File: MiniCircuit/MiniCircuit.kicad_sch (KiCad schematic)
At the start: 32 parts, among them IC1 MAX4737EUD+, IC2 MAX4737EUD+, IC3 MAX4737EUD+, IC4 MAX4737EUD+, J1 Conn_02x16_Odd_Even, J2 Conn_01x08, SW1 SW_DIP_x08, U1 LM6172, U2 OPA2277, U3 MCP3008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

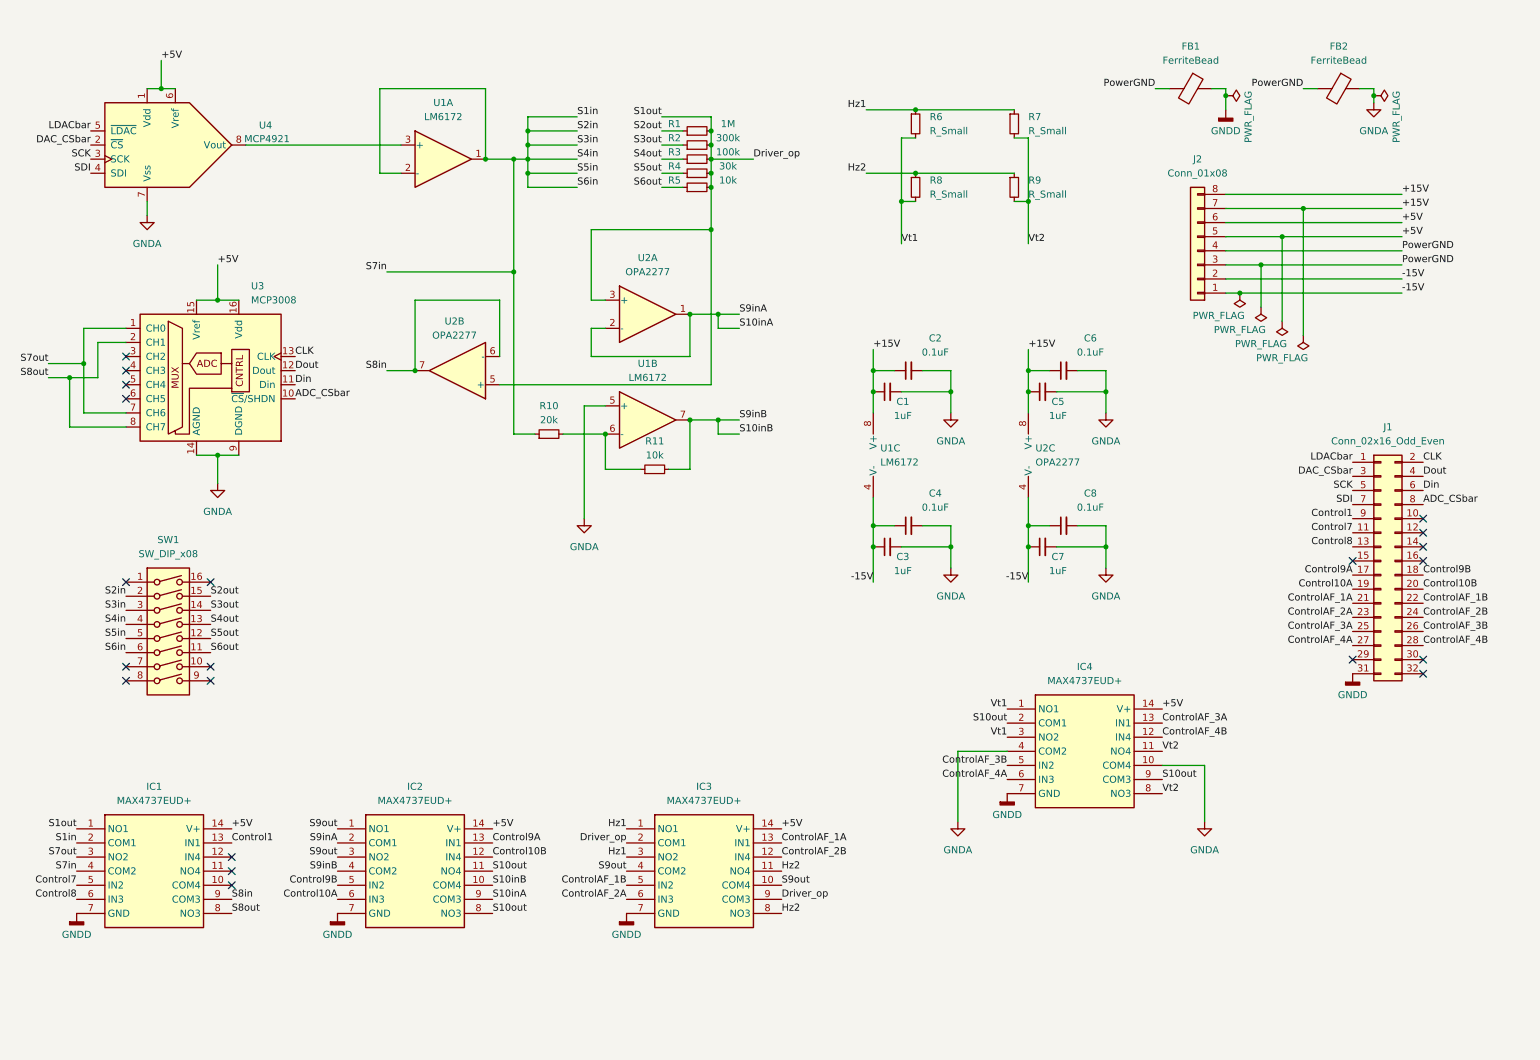
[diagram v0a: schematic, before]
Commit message: Everything done except routing of digital signals and adding Vias
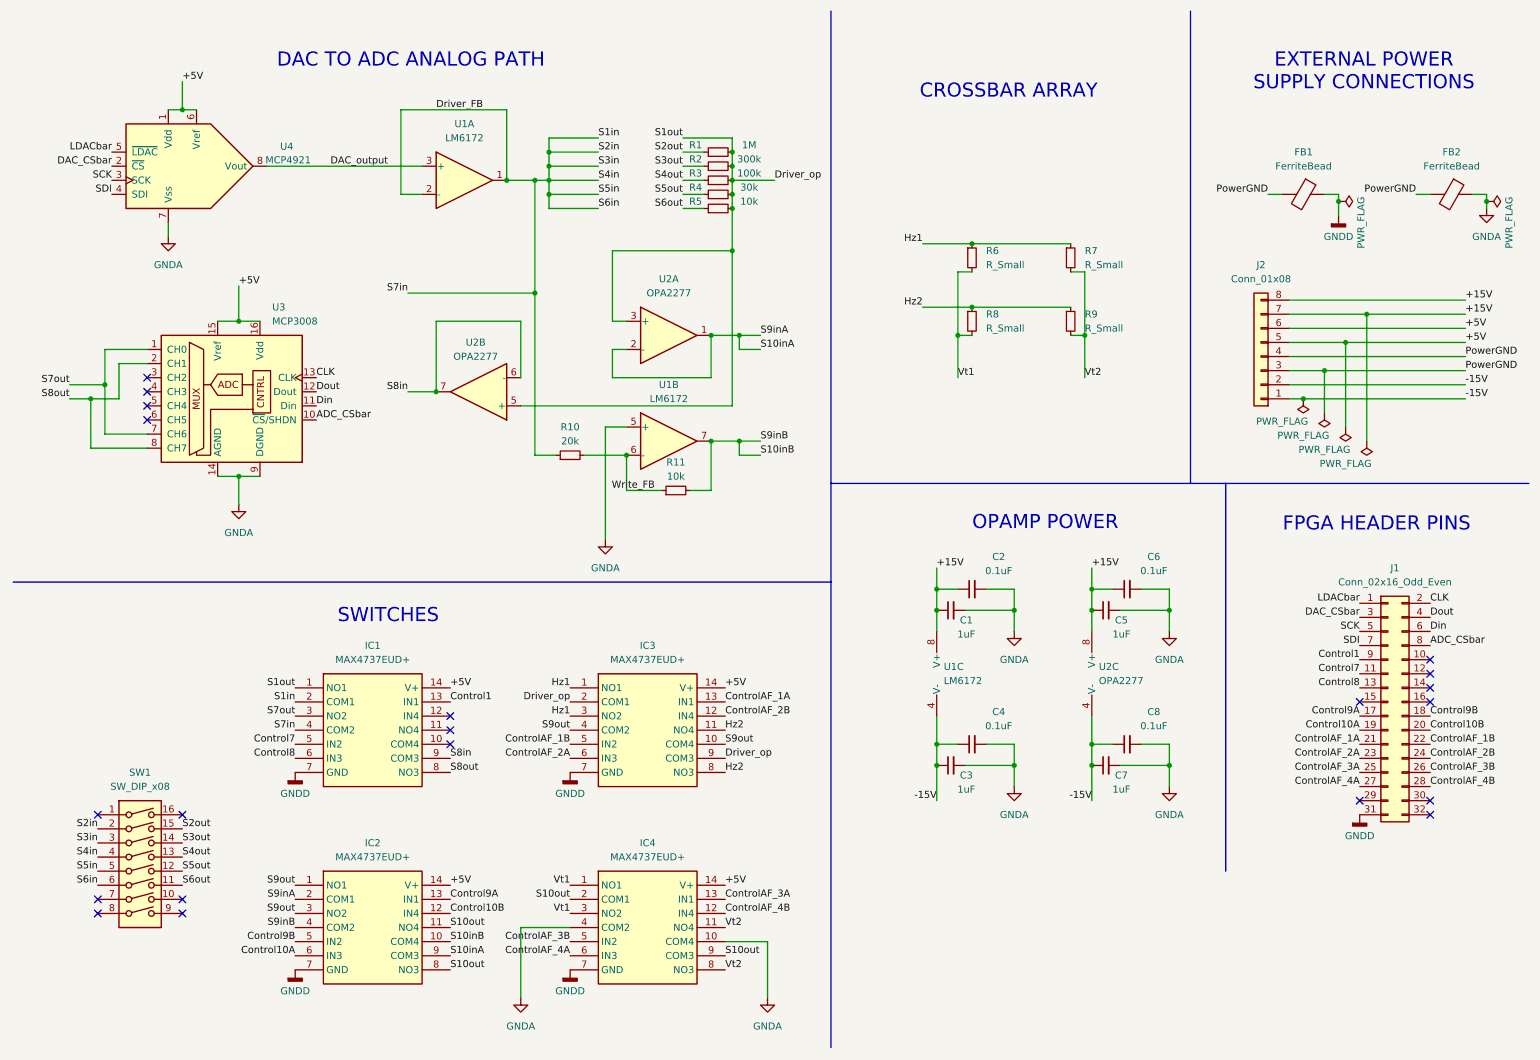
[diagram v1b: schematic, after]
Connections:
- net DAC_output: now reaches U1.3 (+), U4.8 (Vout)
- net Write_FB: now reaches R10.2, R11.1, U1.6 (-)
- net S1in renamed Driver_FB
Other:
- note added: "CROSSBAR ARRAY"
- note added: "DAC TO ADC ANALOG PATH"
- note added: "EXTERNAL POWER SUPPLY CONNECTIONS"
- note added: "FPGA HEADER PINS"
- note added: "OPAMP POWER"
- note added: "SWITCHES"
- moved on the sheet: C1, C2, C3, C4, C5, C6, C7, C8, FB1, FB2, IC1, IC2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

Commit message: Changed Schematic to include CD4066 instead of MAX4737. Design Constraints, Routing and Layout remaining
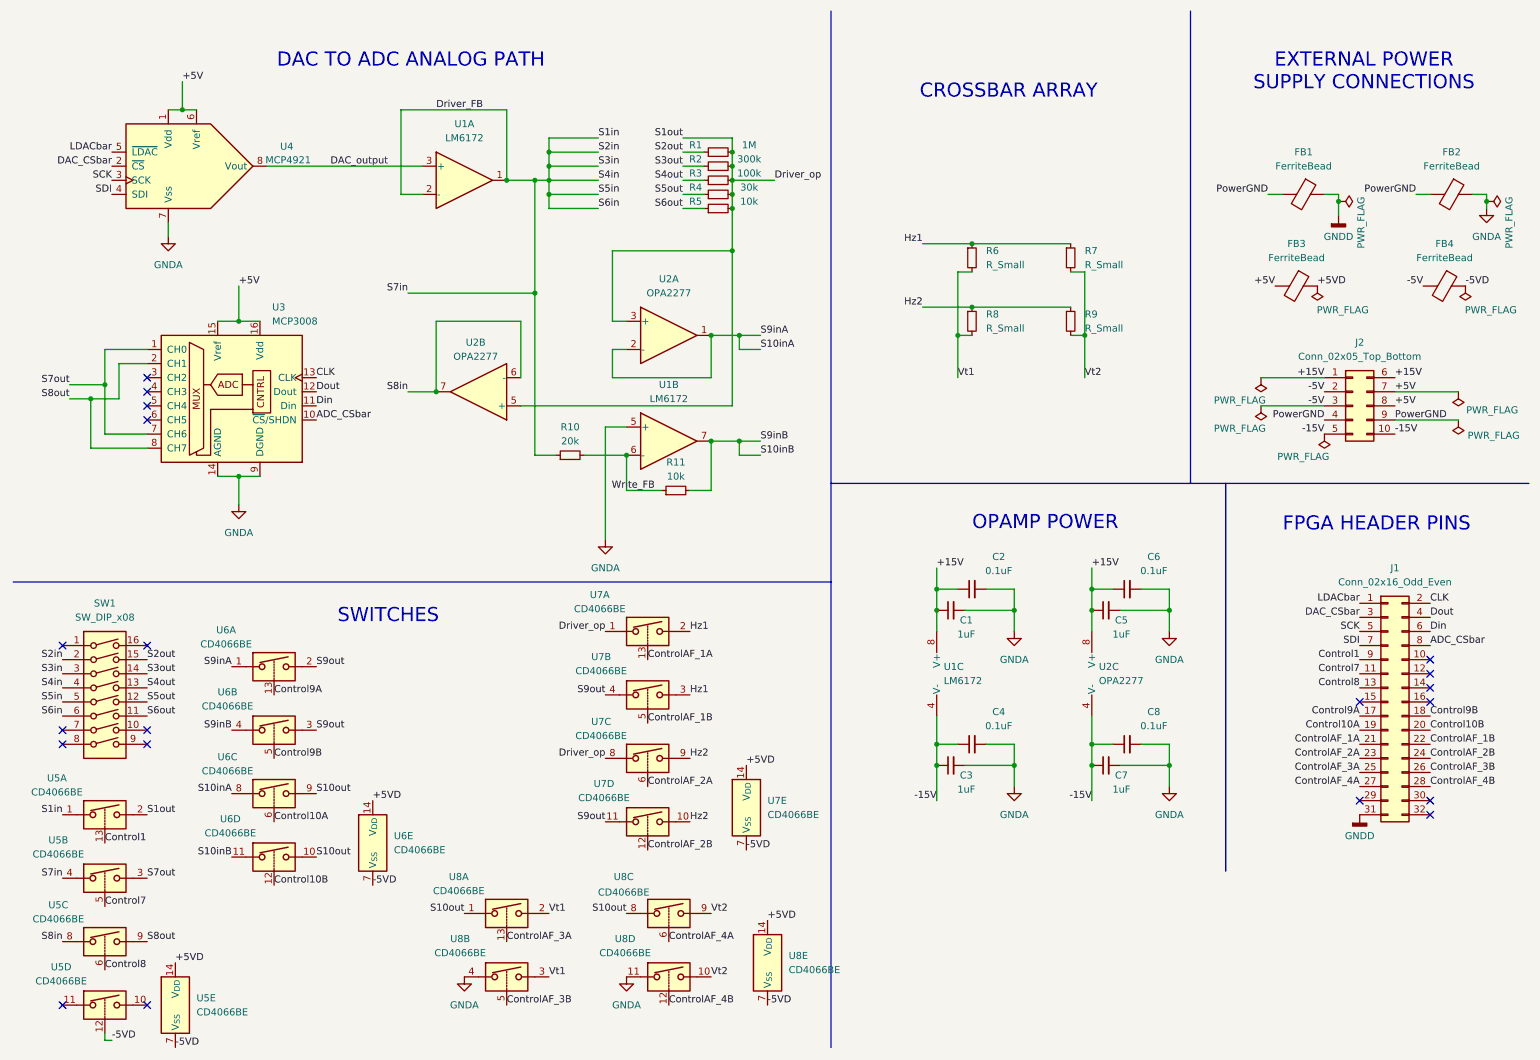
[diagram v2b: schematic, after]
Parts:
- removed IC1, IC2, IC3, IC4: MAX4737EUD+, MAX4737:SOP65P640X110-14N, symbol MAX4737:MAX4737EUD+
- removed J2: Conn_01x08, Connector_PinHeader_2.54mm:PinHeader_1x08_P2.54mm_Vertical, symbol Connector_Generic:Conn_01x08
- added FB3, FB4: FerriteBead, Inductor_SMD:L_1206_3216Metric_Pad1.22x1.90mm_HandSolder, symbol Device:FerriteBead
- added J2: Conn_02x05_Top_Bottom, Connector_PinHeader_2.54mm:PinHeader_2x05_P2.54mm_Vertical, symbol Connector_Generic:Conn_02x05_Top_Bottom
- added U5, U6, U7, U8: CD4066BE, Package_DIP:DIP-14_W7.62mm_Socket, symbol Analog_Switch:CD4066BE
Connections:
- net +15V: now also J2.1 (Pin_1), J2.6 (Pin_6)
- net +5V: now also FB3.2, J2.7 (Pin_7), J2.8 (Pin_8)
- net -15V: now also J2.10 (Pin_10), J2.5 (Pin_5)
- net Control1: now also U5.13
- net Control10A: now also U6.6
- net Control10B: now also U6.12
- net Control7: now also U5.5
- net Control8: now also U5.6
- net Control9A: now also U6.13
- net Control9B: now also U6.5
- net ControlAF_1A: now also U7.13
- net ControlAF_1B: now also U7.5
- net ControlAF_2A: now also U7.6
- net ControlAF_2B: now also U7.12
- net ControlAF_3A: now also U8.13
- net ControlAF_3B: now also U8.5
- net ControlAF_4A: now also U8.6
- net ControlAF_4B: now also U8.12
- net Driver_FB: now also U5.1, U5.4
- net Driver_op: now also U5.2, U7.1, U7.8
- net GNDA: now also U8.11, U8.4
- net Hz1: now also U7.2, U7.3
- net Hz2: now also U7.10, U7.9
- net PowerGND: now also J2.4 (Pin_4), J2.9 (Pin_9)
- net S10inA: now also U6.1, U6.8
- net S10inB: now also U6.11, U6.4
- net S10out: now also U6.10, U6.9, U8.1, U8.8
- net S7out: now also U5.3
- net S8in: now also U5.8
- net S8out: now also U5.9
- net S9out: now also U6.2, U6.3, U7.11, U7.4
- net Vt1: now also U8.2, U8.3
- net Vt2: now also U8.10, U8.9
- new net +5VD: FB3.1, U5.14 (V_{DD}), U6.14 (V_{DD}), U7.14 (V_{DD}), U8.14 (V_{DD})
- new net -5V: FB4.2, J2.2 (Pin_2), J2.3 (Pin_3)
- new net -5VD: FB4.1, U5.12, U5.7 (V_{SS}), U6.7 (V_{SS}), U7.7 (V_{SS}), U8.7 (V_{SS})
- no-connect marks 21 -> 20
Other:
- moved on the sheet: SW1

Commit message: PCB Done, only final touch and verification necessary
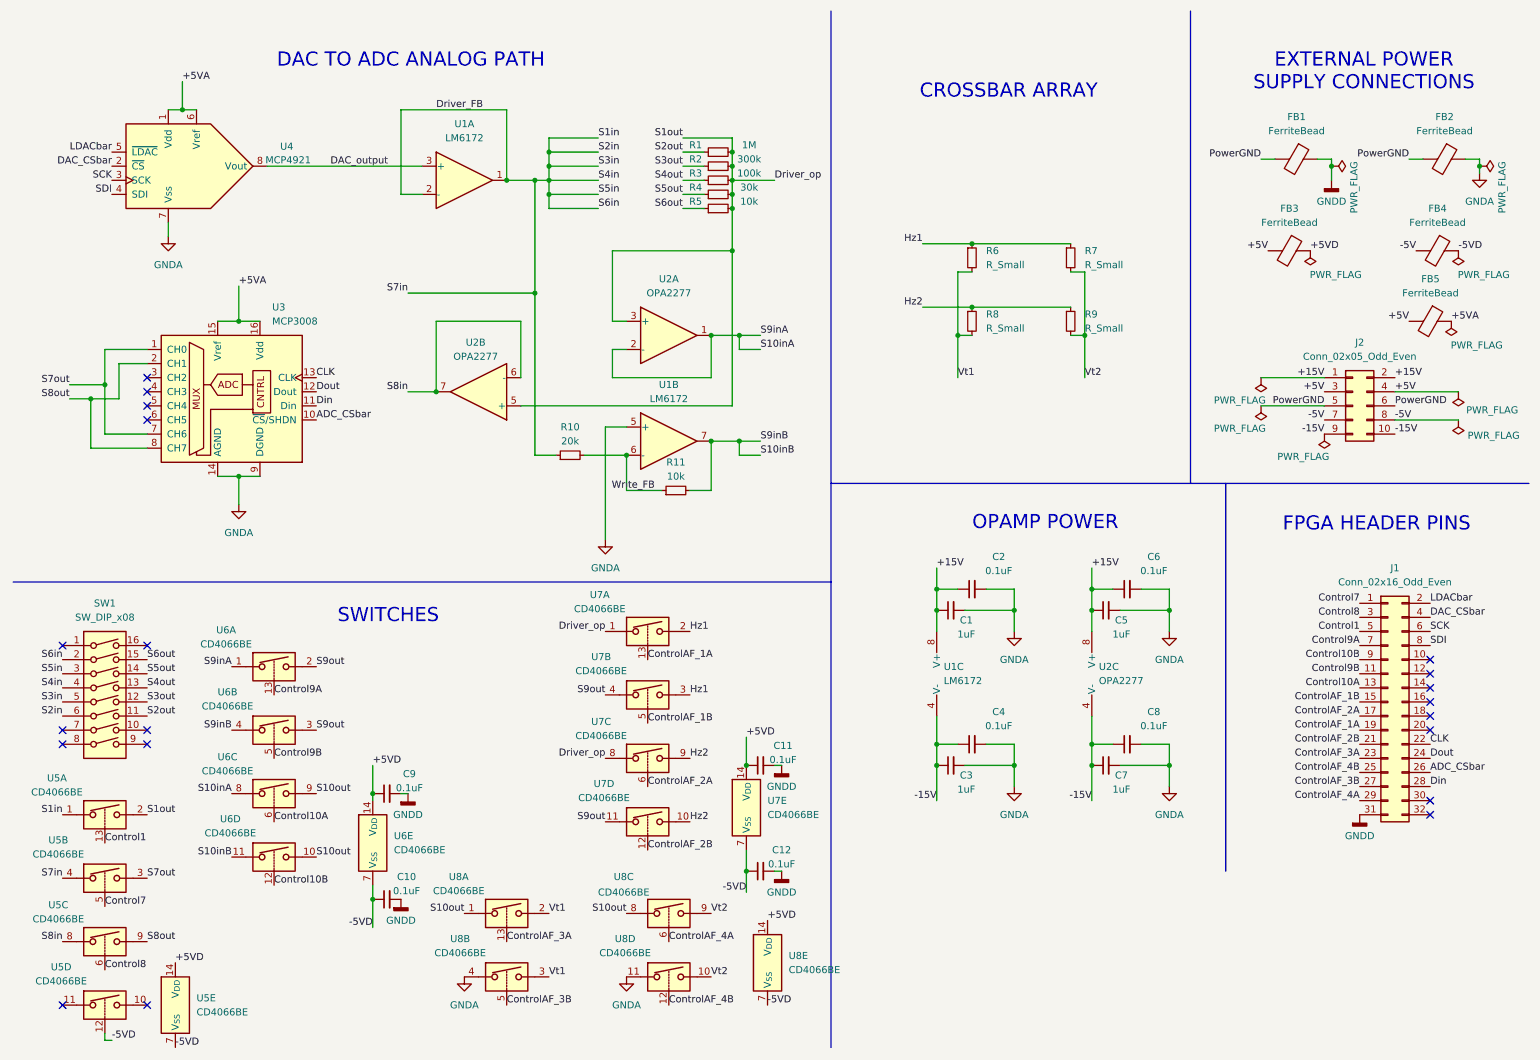
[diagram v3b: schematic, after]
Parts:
- removed J2: Conn_02x05_Top_Bottom, Connector_PinHeader_2.54mm:PinHeader_2x05_P2.54mm_Vertical, symbol Connector_Generic:Conn_02x05_Top_Bottom
- added C10, C11, C12, C9: 0.1uF, Capacitor_SMD:C_1206_3216Metric_Pad1.33x1.80mm_HandSolder, symbol Device:C_Small
- added FB5: FerriteBead, Inductor_SMD:L_1206_3216Metric_Pad1.22x1.90mm_HandSolder, symbol Device:FerriteBead
- added J2: Conn_02x05_Odd_Even, Connector_PinHeader_2.54mm:PinHeader_2x05_P2.54mm_Vertical, symbol Connector_Generic:Conn_02x05_Odd_Even
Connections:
- net +15V: now also J2.1 (Pin_1), J2.2 (Pin_2)
- net +5V: now also FB5.2, J2.3 (Pin_3), J2.4 (Pin_4); no longer U3.15 (Vref), U3.16 (Vdd), U4.1 (Vdd), U4.6 (Vref)
- net +5VD: now also C11.1, C9.1
- net -15V: now also J2.10 (Pin_10), J2.9 (Pin_9)
- net -5V: now also J2.7 (Pin_7), J2.8 (Pin_8)
- net -5VD: now also C10.1, C12.1
- net ADC_CSbar: now also J1.26 (Pin_26); no longer J1.8 (Pin_8)
- net CLK: now also J1.22 (Pin_22); no longer J1.2 (Pin_2)
- net Control1: now also J1.5 (Pin_5); no longer J1.9 (Pin_9)
- net Control10A: now also J1.13 (Pin_13); no longer J1.19 (Pin_19)
- net Control10B: now also J1.9 (Pin_9); no longer J1.20 (Pin_20)
- net Control7: now also J1.1 (Pin_1); no longer J1.11 (Pin_11)
- net Control8: now also J1.3 (Pin_3); no longer J1.13 (Pin_13)
- net Control9A: now also J1.7 (Pin_7); no longer J1.17 (Pin_17)
- net Control9B: now also J1.11 (Pin_11); no longer J1.18 (Pin_18)
- net ControlAF_1A: now also J1.19 (Pin_19); no longer J1.21 (Pin_21)
- net ControlAF_1B: now also J1.15 (Pin_15); no longer J1.22 (Pin_22)
- net ControlAF_2A: now also J1.17 (Pin_17); no longer J1.23 (Pin_23)
- net ControlAF_2B: now also J1.21 (Pin_21); no longer J1.24 (Pin_24)
- net ControlAF_3A: now also J1.23 (Pin_23); no longer J1.25 (Pin_25)
- net ControlAF_3B: now also J1.27 (Pin_27); no longer J1.26 (Pin_26)
- net ControlAF_4A: now also J1.29 (Pin_29); no longer J1.27 (Pin_27)
- net ControlAF_4B: now also J1.25 (Pin_25); no longer J1.28 (Pin_28)
- net DAC_CSbar: now also J1.4 (Pin_4); no longer J1.3 (Pin_3)
- net Din: now also J1.28 (Pin_28); no longer J1.6 (Pin_6)
- net Dout: now also J1.24 (Pin_24); no longer J1.4 (Pin_4)
- net GNDD: now also C10.2, C11.2, C12.2, C9.2
- net LDACbar: now also J1.2 (Pin_2); no longer J1.1 (Pin_1)
- net PowerGND: now also J2.5 (Pin_5), J2.6 (Pin_6)
- net S2out: now also SW1.11; no longer SW1.15
- net S3out: now also SW1.12; no longer SW1.14
- net S5out: now also SW1.14; no longer SW1.12
- net S6out: now also SW1.15; no longer SW1.11
- net SCK: now also J1.6 (Pin_6); no longer J1.5 (Pin_5)
- net SDI: now also J1.8 (Pin_8); no longer J1.7 (Pin_7)
- new net +5VA: FB5.1, U3.15 (Vref), U3.16 (Vdd), U4.1 (Vdd), U4.6 (Vref)
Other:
- moved on the sheet: FB1, FB2, FB3, FB4

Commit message: PCB Complete. Self verification left.
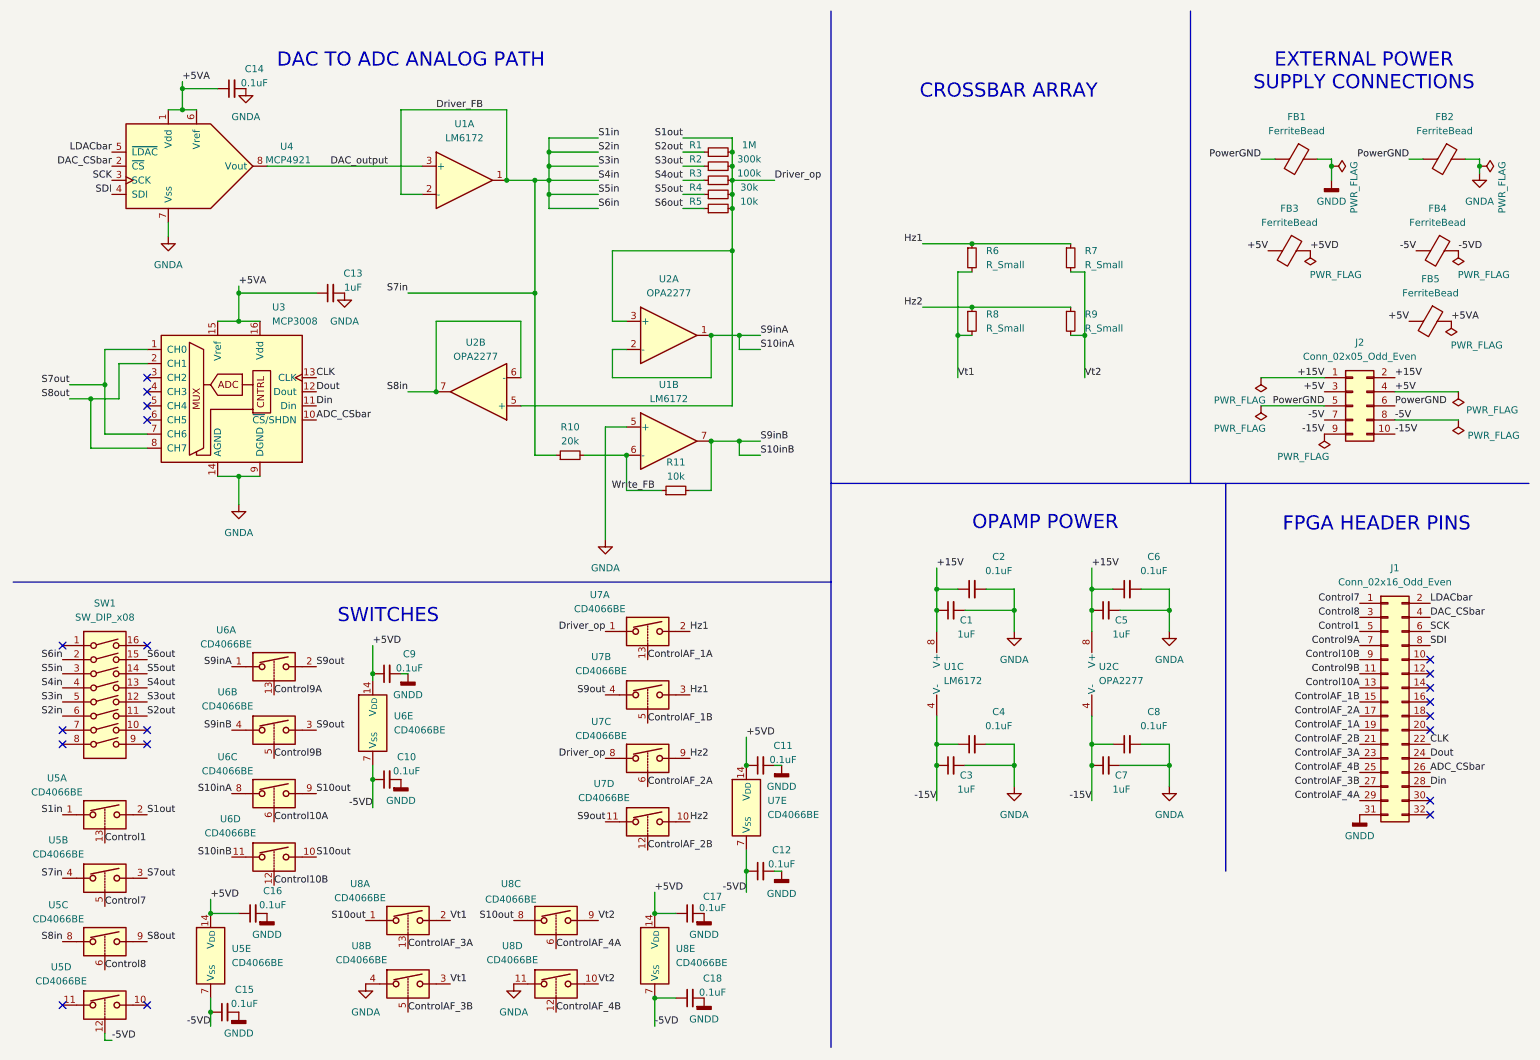
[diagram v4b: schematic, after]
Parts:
- added C13: 1uF, Capacitor_SMD:C_1206_3216Metric_Pad1.33x1.80mm_HandSolder, symbol Device:C_Small
- added C14, C15, C16, C17, C18: 0.1uF, Capacitor_SMD:C_1206_3216Metric_Pad1.33x1.80mm_HandSolder, symbol Device:C_Small
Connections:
- net +5VA: now also C13.1, C14.1
- net +5VD: now also C16.1, C17.1
- net -5VD: now also C15.1, C18.1
- net GNDA: now also C13.2, C14.2
- net GNDD: now also C15.2, C16.2, C17.2, C18.2
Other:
- moved on the sheet: C10, C9, U5E, U6E, U8A, U8B, U8C, U8D, U8E
